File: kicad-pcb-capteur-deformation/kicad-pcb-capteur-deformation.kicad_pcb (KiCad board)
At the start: 2 copper layers, 68.6 x 53.3 mm, 10 parts, among them J1 Power, J2 Digital/PWM, J3 Analog, J4 Digital/PWM

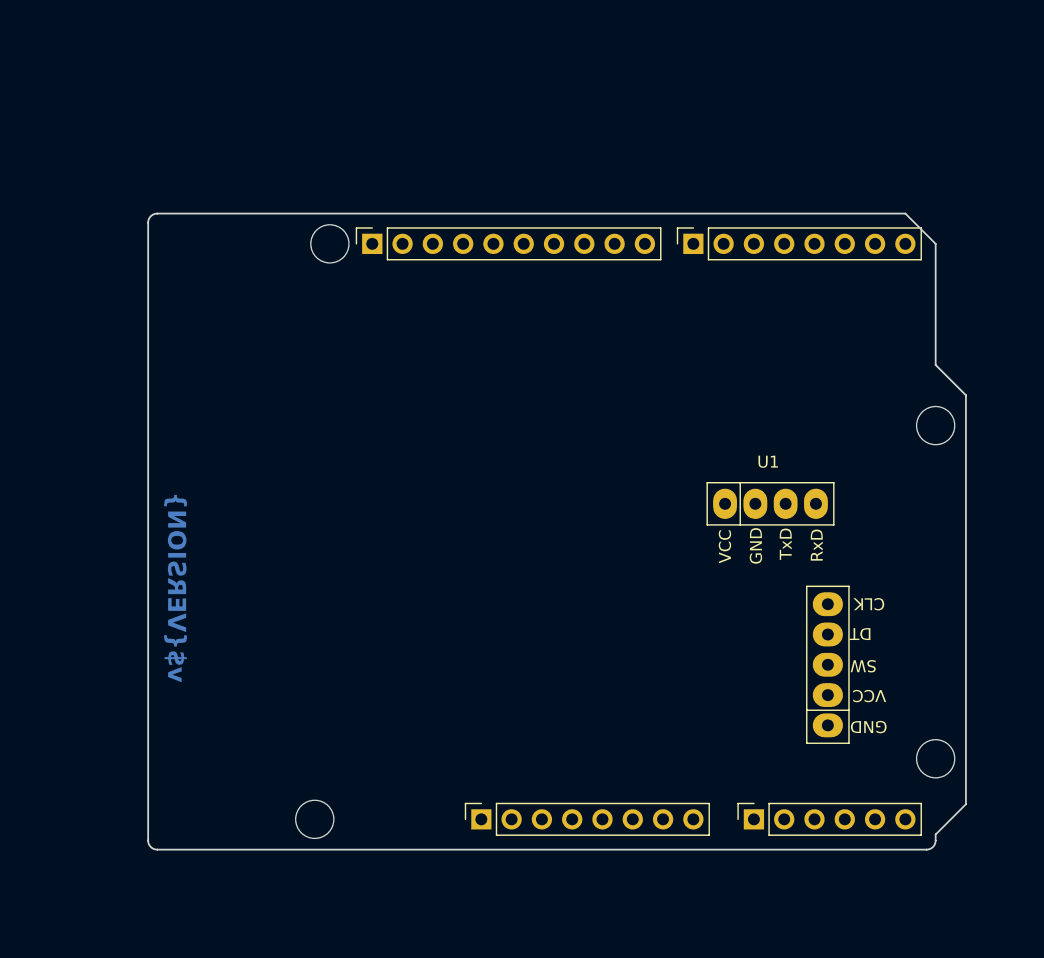
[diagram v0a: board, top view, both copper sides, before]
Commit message: empreintes et début de wiring KiCad
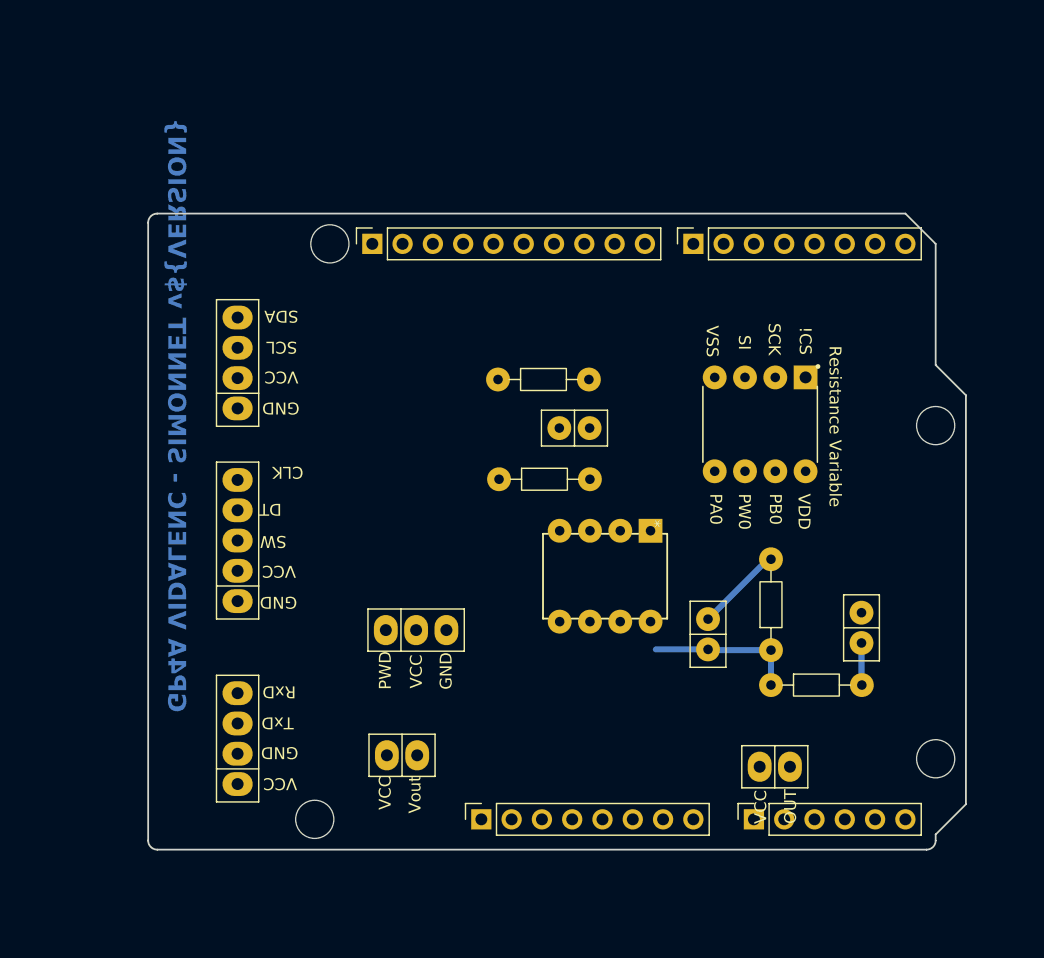
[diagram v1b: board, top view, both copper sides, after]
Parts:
- removed REF**: encodeur_rotatoire, capteur_graphite_lib:encodeur_rotatoire
- added C1: 2u, capteur_graphite_lib:C, F.Cu at (146.9, 81.9)
- added C2: 100n, capteur_graphite_lib:C, F.Cu at (159.8, 81.4)
- added C4: 100n, capteur_graphite_lib:C, F.Cu at (135.8, 64.7)
- added M1: Servo Moteur, capteur_graphite_lib:Servo Moteur, F.Cu at (122.5, 81.6)
- added R1: 100k, capteur_graphite_lib:R, F.Cu at (152.2, 83.3)
- added R2: 1k, capteur_graphite_lib:R, F.Cu at (152.2, 86.2)
- added R3: 100k, capteur_graphite_lib:R, F.Cu at (129.4, 68.9)
- added R4: 10k, capteur_graphite_lib:R, F.Cu at (129.3, 60.6)
- added U2: Encodeur, capteur_graphite_lib:encodeur_rotatoire, F.Cu at (107.5, 74.1)
- added U3: LTC1050CN8_PBF, capteur_graphite_lib:LTC-1050, F.Cu at (134.5, 80.9)
- added U4: OLED, capteur_graphite_lib:OLED SSD1306, F.Cu at (107.5, 59.2)
- added U5: MCP41010-I_P, capteur_graphite_lib:Resistance Variable, F.Cu at (151.3, 64.3)
- added U6: Capteur, capteur_graphite_lib:Capteur, F.Cu at (121.3, 92.1)
- added U7: Flex, capteur_graphite_lib:Flex Sensor, F.Cu at (152.6, 93.0)
- U1: value ~ -> Bluetooth HC05
- moved U1 48.8 mm to (107.5, 90.7), turned to 90 degrees
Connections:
- net /SCL/A5 renamed SCL
- net /SDA/A4 renamed SDA
- J2 pad 5: /13 -> SCK
- J2 pad 7: /*11 -> MOSI
- J2 pad 8: /*10 -> SS
- J2 pad 9: /*9 -> PWM
- J3 pad 2: /A1 -> FLX
- J4 pad 3: /*5 -> SW
- J4 pad 4: /4 -> DT
- J4 pad 6: /2 -> CLK
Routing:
- net Net-(U3-OUT): track 0.00 -> 12.6 mm
- net PB0: track 0.00 -> 7.36 mm
- net Net-(C2-Pad1): track 0.00 -> 3.54 mm
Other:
- board text added: "GP4A VIDALENC - SIMONNET v${VERSION}"
- board text removed: "v${VERSION}"

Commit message: PCB fini
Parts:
- added R5: 47k, capteur_graphite_lib:R, F.Cu at (153.5, 89.0)
- M1: value Servo Moteur -> Motor_Servo
- U1: value Bluetooth HC05 -> Bluetotth HC05
- U4: value OLED -> ~
- moved U2 52.5 mm to (157.0, 56.6), turned to 0 degrees
- moved U1 47.9 mm to (143.7, 59.4)
- moved M1 26.3 mm to (136.0, 59.0), turned to -90 degrees
- moved U5 26.2 mm to (125.1, 63.9)
- moved R4 20.7 mm to (117.5, 77.6), turned to -90 degrees
- moved C4 20.4 mm to (121.1, 78.8), turned to -90 degrees
- moved R3 16.7 mm to (125.4, 85.1), turned to 90 degrees
- moved U3 4.97 mm to (139.4, 81.8), turned to 0 degrees
- moved C2 4.57 mm to (157.4, 77.5)
- moved R2 4.57 mm to (149.8, 82.3)
- moved R1 4.57 mm to (149.8, 79.4)
- moved C1 4.31 mm to (145.2, 78.0)
- moved U4 2.57 mm to (107.8, 61.7), turned to -90 degrees
- moved U6 2.06 mm to (120.7, 90.1), turned to 180 degrees
- moved U7 0.53 mm to (152.1, 93.2)
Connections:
- C2 pad 1: Net-(C2-Pad1) -> Signal
- J1 pad 5: +5V -> VCC
- J1 pad 8: VCC -> VCC_Arduino
- J3 pad 3: /A2 -> Signal
- R2 pad 2: Net-(C2-Pad1) -> Signal
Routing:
- net VCC: track 0.00 -> 204.4 mm, vias 0 -> 2
- net PB0: track 7.36 -> 42.2 mm
- net SDA: track 0.00 -> 22.1 mm
- net GND: track 0.00 -> 21.5 mm
- net Signal: track 0.00 -> 19.3 mm, vias 0 -> 2
- net SCL: track 0.00 -> 19.2 mm
- net MOSI: track 0.00 -> 16.8 mm, vias 0 -> 2
- net Net-(U3-+IN): track 0.00 -> 15.1 mm
- net SS: track 0.00 -> 13.9 mm
- net SCK: track 0.00 -> 11.8 mm
- net SW: track 0.00 -> 10.0 mm
- net DT: track 0.00 -> 10.0 mm
- net TxD: track 0.00 -> 9.89 mm
- net CLK: track 0.00 -> 8.97 mm
- net FLX: track 0.00 -> 8.55 mm
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- added copper zone on B.Cu, net GND
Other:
- outline, holes or cut-outs redrawn

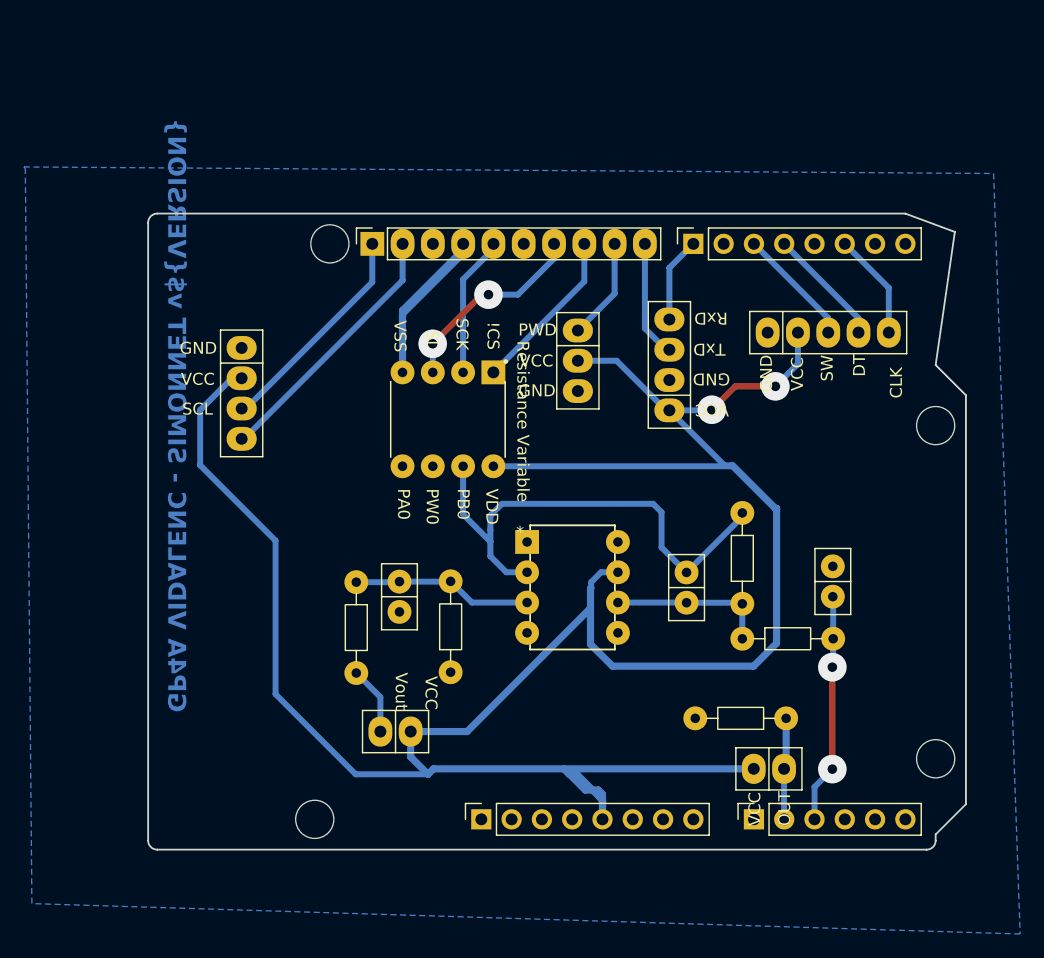
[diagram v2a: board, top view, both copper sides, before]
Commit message: maj des fichiers KiCad, VF préliminaire
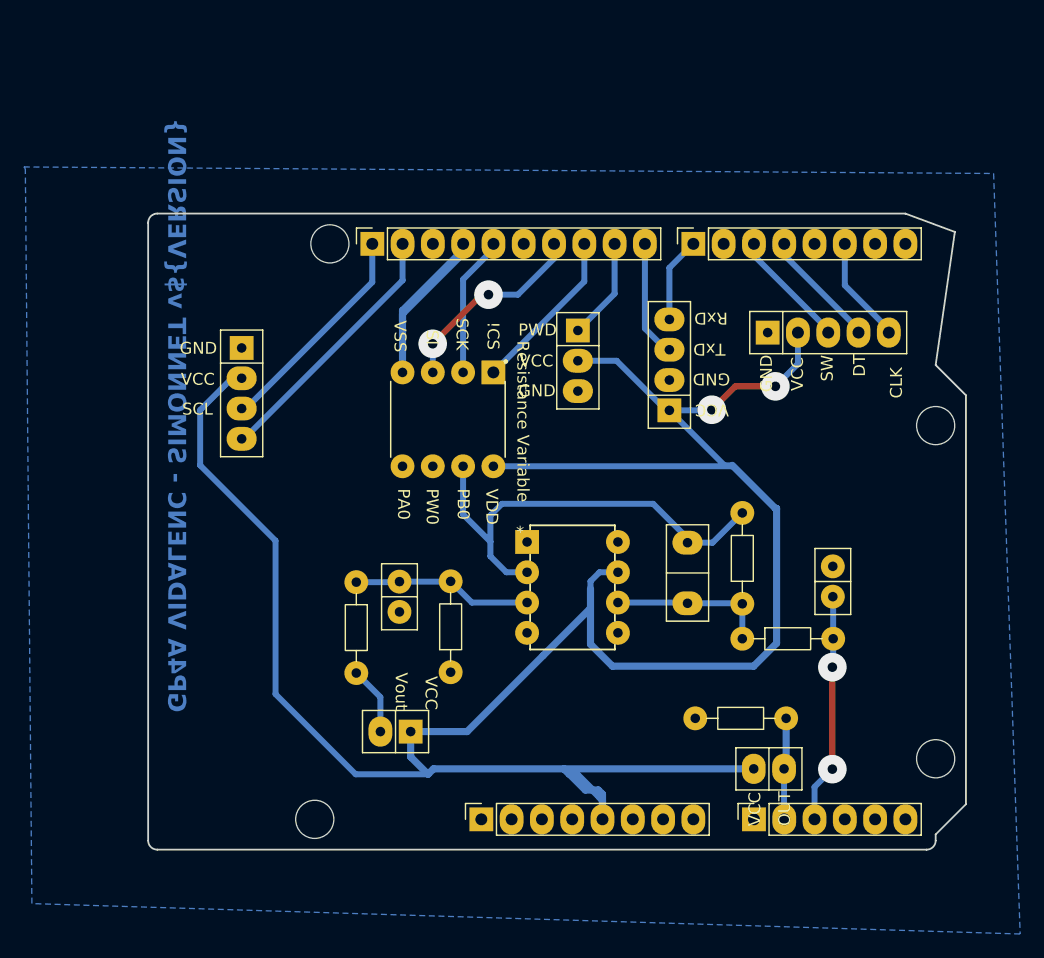
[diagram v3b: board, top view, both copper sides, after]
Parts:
- C1: value 2u -> 1u; footprint capteur_graphite_lib:C -> capteur_graphite_lib:C - 5,08
- moved C1 1.23 mm to (145.2, 76.8)
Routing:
- net PB0: track 42.2 -> 38.8 mm
